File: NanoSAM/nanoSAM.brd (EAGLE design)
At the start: 95.9 x 90.2 mm, 90 parts, among them J1 POWER_JACK, U1 LTC3260EMSEPBF, U2 LMV324

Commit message: added some stuff, fixed some stuff
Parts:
- added C17, C18: 0.1uF, SparkFun-Capacitors:0603
- added C19, C20: .1uF, SparkFun-Capacitors:0603
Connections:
- net +3V3: now also C19.1, C20.2
- net -5V: now also C18.1
- net 5V: now also C17.1
- net AGND: now also C17.2, C18.2
- net DGND: now also C19.2, C20.1
- net SPI_MISO: now also U$16.2, U$17.2; no longer U$16.5, U$17.5
- net SPI_MOSI: now also U$16.5, U$17.5; no longer U$16.6, U$17.6
- net SPI_SCK: now also U$16.6, U$17.6; no longer U$16.2, U$17.2
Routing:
- net SPI_MISO: track 53.8 -> 44.6 mm
- net SPI_SCK: track 88.4 -> 84.6 mm
- net SPI_MOSI: track 26.9 -> 25.4 mm
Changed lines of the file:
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@@
 <attribute name="VALUE" x="72.957" y="65.8" size="0.6096" layer="27" font="vector" ratio="20" rot="R270" align="top-center"/>
+</element>
+<element name="C17" library="SparkFun-Capacitors" library_urn="urn:adsk.eagle:library:510" package="0603" package3d_urn="urn:adsk.eagle:package:37414/1" value="0.1uF" x="-19" y="-2" smashed="yes">
+<attribute name="NAME" x="-19" y="-1.238" size="0.6096" layer="25" font="vector" ratio="20" align="bottom-center"/>
+<attribute name="PROD_ID" value="CAP-08604" x="-19" y="-2" size="1.778" layer="27" display="off"/>
+<attribute name="VALUE" x="-19" y="-2.762" size="0.6096" layer="27" font="vector" ratio="20" align="top-center"/>
+</element>
+<element name="C18" library="SparkFun-Capacitors" library_urn="urn:adsk.eagle:library:510" package="0603" package3d_urn="urn:adsk.eagle:package:37414/1" value="0.1uF" x="-19" y="-6" smashed="yes">
+<attribute name="NAME" x="-19" y="-5.238" size="0.6096" layer="25" font="vector" ratio="20" align="bottom-center"/>
+<attribute name="PROD_ID" value="CAP-08604" x="-19" y="-6" size="1.778" layer="27" display="off"/>
+<attribute name="VALUE" x="-19" y="-6.762" size="0.6096" layer="27" font="vector" ratio="20" align="top-center"/>
+</element>
+<element name="C19" library="SparkFun-Capacitors" library_urn="urn:adsk.eagle:library:510" package="0603" package3d_urn="urn:adsk.eagle:package:37414/1" value=".1uF" x="-19" y="-10" smashed="yes">
+<attribute name="NAME" x="-19" y="-9.238" size="0.6096" layer="25" font="vector" ratio="20" align="bottom-center"/>
+<attribute name="PROD_ID" value="CAP-08604" x="-19" y="-10" size="1.778" layer="27" display="off"/>
+<attribute name="VALUE" x="-19" y="-10.762" size="0.6096" layer="27" font="vector" ratio="20" align="top-center"/>
+</element>
+<element name="C20" library="SparkFun-Capacitors" library_urn="urn:adsk.eagle:library:510" package="0603" package3d_urn="urn:adsk.eagle:package:37414/1" value=".1uF" x="-19" y="-14" smashed="yes">
+<attribute name="NAME" x="-19" y="-13.238" size="0.6096" layer="25" font="vector" ratio="20" align="bottom-center"/>
+<attribute name="PROD_ID" value="CAP-08604" x="-19" y="-14" size="1.778" layer="27" display="off"/>
+<attribute name="VALUE" x="-19" y="-14.762" size="0.6096" layer="27" font="vector" ratio="20" align="top-center"/>
 </element>
 </elements>
@@
 <contactref element="U$5" pad="P6"/>
 <contactref element="U$2" pad="D12"/>
-<contactref element="U$16" pad="5"/>
-<contactref element="U$17" pad="5"/>
-<wire x1="61.07" y1="71.925" x2="52" y2="71.925" width="0.254" layer="1"/>
 <wire x1="52" y1="71.925" x2="39.975" y2="71.925" width="0.254" layer="1"/>
 <wire x1="39.975" y1="71.925" x2="39.5" y2="72.4" width="0.254" layer="1"/>
@@
 <wire x1="54" y1="69.925" x2="54" y2="66" width="0.254" layer="1"/>
 <wire x1="54" y1="66" x2="56" y2="64" width="0.254" layer="1"/>
-<wire x1="61.135" y1="64" x2="61.21" y2="63.925" width="0.254" layer="1"/>
 <wire x1="56" y1="64" x2="61.135" y2="64" width="0.254" layer="1"/>
 <wire x1="51.14" y1="52.43" x2="54" y2="55.29" width="0.254" layer="1"/>
 <wire x1="54" y1="55.29" x2="54" y2="66" width="0.254" layer="1"/>
+<contactref element="U$16" pad="2"/>
+<contactref element="U$17" pad="2"/>
+<wire x1="67.87" y1="61.385" x2="67.73" y2="69.385" width="0" layer="19" extent="1-1"/>
+<wire x1="61.135" y1="64" x2="67.87" y2="61.385" width="0" layer="19" extent="1-1"/>
 </signal>
 <signal name="SPI_SCK">
 <contactref element="U$5" pad="P5"/>
 <contactref element="U$2" pad="D13/LED"/>
-<contactref element="U$16" pad="2"/>
-<contactref element="U$17" pad="2"/>
-<wire x1="67.73" y1="69.385" x2="69.615" y2="69.385" width="0.254" layer="1"/>
 <wire x1="69.615" y1="69.385" x2="70" y2="69" width="0.254" layer="1"/>
 <wire x1="70" y1="69" x2="70" y2="61.6" width="0.254" layer="1"/>
@@
 <wire x1="51.14" y1="38.14" x2="51.14" y2="37.19" width="0.254" layer="1"/>
 <wire x1="70" y1="51" x2="58" y2="39" width="0.254" layer="1"/>
-<wire x1="67.87" y1="61.385" x2="69.785" y2="61.385" width="0.254" layer="1"/>
 <wire x1="69.785" y1="61.385" x2="70" y2="61.6" width="0.254" layer="1"/>
 <wire x1="70" y1="69" x2="70" y2="73" width="0.254" layer="1"/>
@@
 <wire x1="36.1" y1="72.33526875" x2="36.1" y2="73.1" width="0.254" layer="1"/>
 <wire x1="69" y1="74" x2="37" y2="74" width="0.254" layer="1"/>
+<contactref element="U$16" pad="6"/>
+<contactref element="U$17" pad="6"/>
+<wire x1="61.21" y1="62.655" x2="61.07" y2="70.655" width="0" layer="19" extent="1-1"/>
+<wire x1="69" y1="74" x2="61.07" y2="70.655" width="0" layer="19" extent="1-1"/>
 </signal>
 <signal name="SPI_MOSI">
 <contactref element="U$2" pad="D11"/>
-<contactref element="U$16" pad="6"/>
-<contactref element="U$17" pad="6"/>
-<wire x1="61.07" y1="70.655" x2="62.345" y2="70.655" width="0.254" layer="1"/>
 <wire x1="62.345" y1="70.655" x2="63" y2="70" width="0.254" layer="1"/>
 <wire x1="63" y1="70" x2="63" y2="63.5" width="0.254" layer="1"/>
 <wire x1="62" y1="62.5" x2="63" y2="63.5" width="0.254" layer="1"/>
 <wire x1="61.365" y1="62.5" x2="62" y2="62.5" width="0.254" layer="1"/>
-<wire x1="61.365" y1="62.5" x2="61.21" y2="62.655" width="0.254" layer="1"/>
 <wire x1="62.42573125" y1="59.5356" x2="60.7856" y2="59.5356" width="0.254" layer="1"/>
 <wire x1="60.7856" y1="59.5356" x2="53.68" y2="52.43" width="0.254" layer="1"/>
 <wire x1="63" y1="63.5" x2="63" y2="60.10986875" width="0.254" layer="1"/>
 <wire x1="63" y1="60.10986875" x2="62.42573125" y2="59.5356" width="0.254" layer="1"/>
+<contactref element="U$16" pad="5"/>
+<contactref element="U$17" pad="5"/>
+<wire x1="62.345" y1="70.655" x2="61.07" y2="71.925" width="0" layer="19" extent="1-1"/>
+<wire x1="61.21" y1="63.925" x2="61.365" y2="62.5" width="0" layer="19" extent="1-1"/>
 </signal>
 <signal name="N$8">
@@
 <wire x1="11.3" y1="39.6" x2="9.71" y2="38.01" width="0.508" layer="16"/>
 <wire x1="6.16" y1="38.01" x2="9.71" y2="38.01" width="0.508" layer="16"/>
+<contactref element="C17" pad="1"/>
+<wire x1="-19.85" y1="-2" x2="6.16" y2="22.24" width="0" layer="19" extent="1-1"/>
 </signal>
 <signal name="AGND">
@@
 <wire x1="14.9" y1="63.1" x2="14.8" y2="63" width="0.508" layer="16"/>
 <wire x1="14.8" y1="63" x2="11.3" y2="63" width="0.508" layer="16"/>
+<contactref element="C17" pad="2"/>
+<contactref element="C18" pad="2"/>
+<wire x1="-18.15" y1="-2" x2="-18.15" y2="-6" width="0" layer="19" extent="1-1"/>
+<wire x1="9.4" y1="11.5" x2="-18.15" y2="-2" width="0" layer="19" extent="1-1"/>
 </signal>
 <signal name="DGND">
@@
 <wire x1="83.265" y1="67.265" x2="83.3" y2="67.3" width="0.254" layer="1"/>
 <via x="83.3" y="67.3" extent="1-16" drill="0.35"/>
+<contactref element="C19" pad="2"/>
+<contactref element="C20" pad="1"/>
 <wire x1="72.6" y1="17.2" x2="71.098" y2="17.768" width="0" layer="19" extent="1-1"/>
+<wire x1="-18.15" y1="-10" x2="32.845" y2="3.68" width="0" layer="19" extent="1-1"/>
+<wire x1="-19.85" y1="-14" x2="-18.15" y2="-10" width="0" layer="19" extent="1-1"/>
 </signal>
 <signal name="+3V3" class="2">
@@
 <wire x1="73.9" y1="67" x2="72" y2="67" width="0.254" layer="1"/>
 <via x="72" y="67" extent="1-16" drill="0.35"/>
+<contactref element="C19" pad="1"/>
+<contactref element="C20" pad="2"/>
+<wire x1="-19.85" y1="-10" x2="-18.15" y2="-14" width="0" layer="19" extent="1-1"/>
+<wire x1="32.3406" y1="3.06426875" x2="-18.15" y2="-14" width="0" layer="19" extent="1-1"/>
 </signal>
 <signal name="VBUS">
@@
 <wire x1="19.9" y1="51.9" x2="20.3" y2="52.3" width="0.508" layer="16"/>
 <wire x1="20.3" y1="52.3" x2="20.3" y2="53" width="0.508" layer="16"/>
+<contactref element="C18" pad="1"/>
+<wire x1="-19.85" y1="-6" x2="19.55" y2="27.61" width="0" layer="19" extent="1-1"/>
 </signal>
 <signal name="N$22">

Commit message: updated some stuff
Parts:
- C1: value 0.1uF -> 100pF
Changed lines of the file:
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@@
 </autorouter>
 <elements>
-<element name="C1" library="SparkFun-Capacitors" library_urn="urn:adsk.eagle:library:510" package="0603" package3d_urn="urn:adsk.eagle:package:37414/1" value="0.1uF" x="21.79" y="72.05" smashed="yes" rot="R270">
+<element name="C1" library="SparkFun-Capacitors" library_urn="urn:adsk.eagle:library:510" package="0603" package3d_urn="urn:adsk.eagle:package:37414/1" value="100pF" x="21.79" y="72.05" smashed="yes" rot="R270">
 <attribute name="NAME" x="20.852" y="75.05" size="1.778" layer="25" font="vector" ratio="20" rot="R270" align="bottom-center"/>
 <attribute name="PROD_ID" value="CAP-08604" x="-37.9" y="53" size="1.778" layer="27" rot="R270" display="off"/>

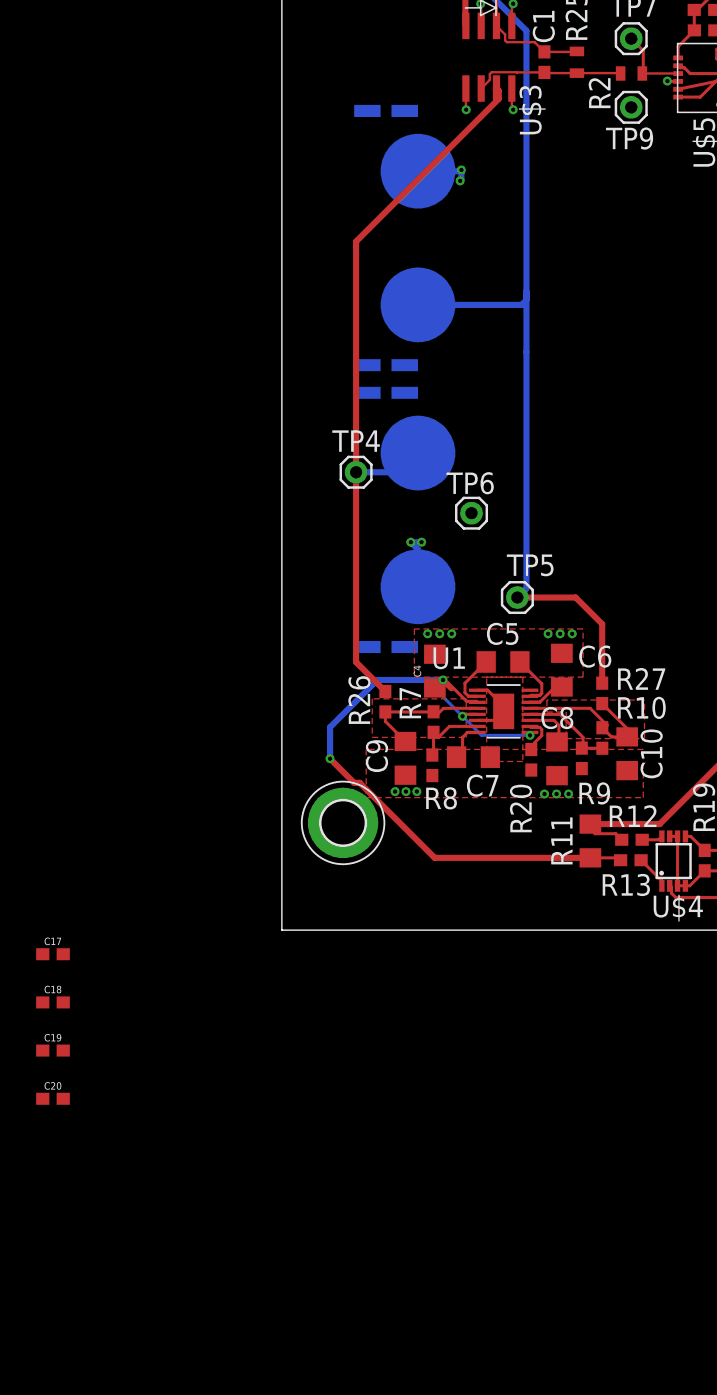
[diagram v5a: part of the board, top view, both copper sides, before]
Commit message: added options for grounding ADCs
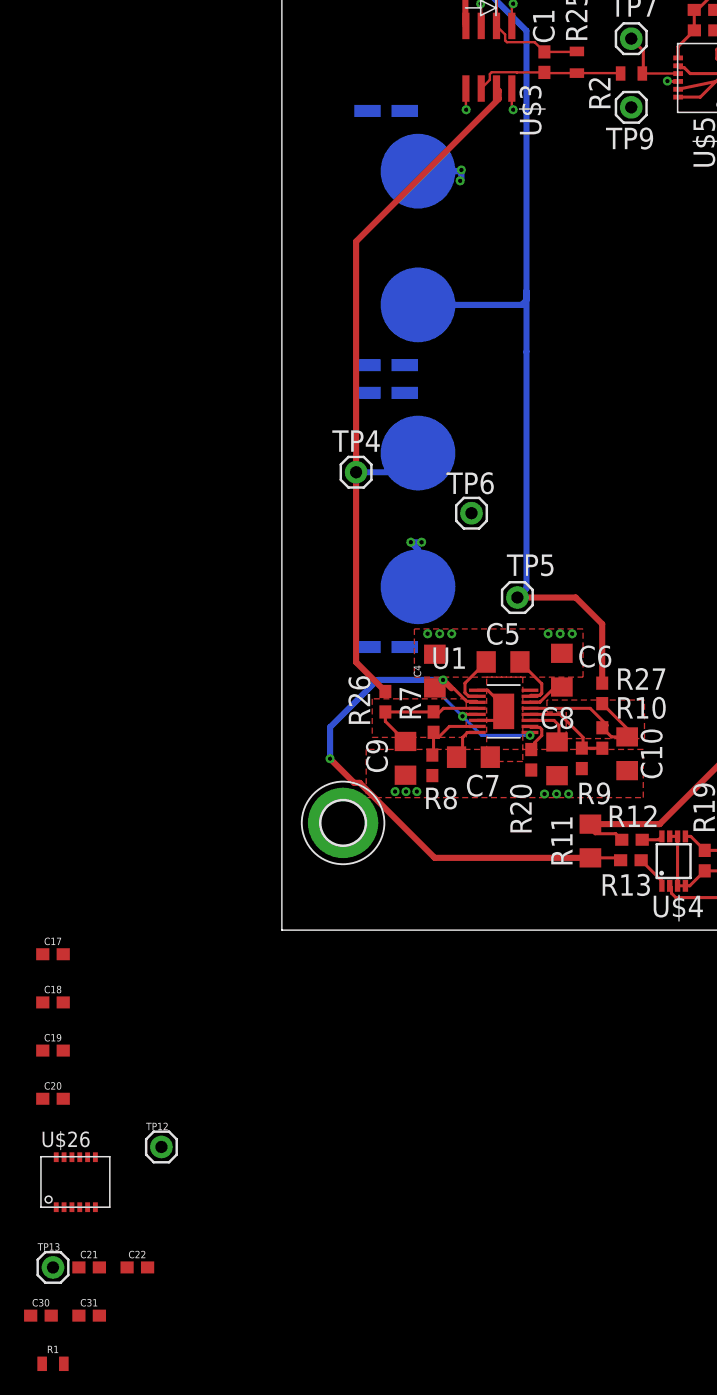
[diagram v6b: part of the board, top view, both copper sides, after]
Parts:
- added C21, C22, C30, C31: 0.1uF, SparkFun-Capacitors:0603
- added R1: 0, SparkFun-Resistors:0805
- added TP12, TP13: (no value), testpoint:1X01
- added U$26: LTC2470, LTC2470:MSOP12
- R2: value (none) -> 0
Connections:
- new net N$25: C21.2, U$26.P1
- new net N$26: C30.1, C31.1, U$26.P7
- new net N$5: R2.2, TP12.1, U$26.P9
- new net N$9: C22.2, U$26.P2
- net ADC_CS: now also U$26.P3
- net AGND: now also C21.1, C22.1, C30.2, C31.2, TP13.1, U$26.P10, U$26.P11, U$26.P12, U$26.P4, U$26.P8
- net N$2: now also R1.1
- net N$3: now also R1.2; no longer R2.2
- net SPI_MISO: now also U$26.P6
- net SPI_SCK: now also U$26.P5

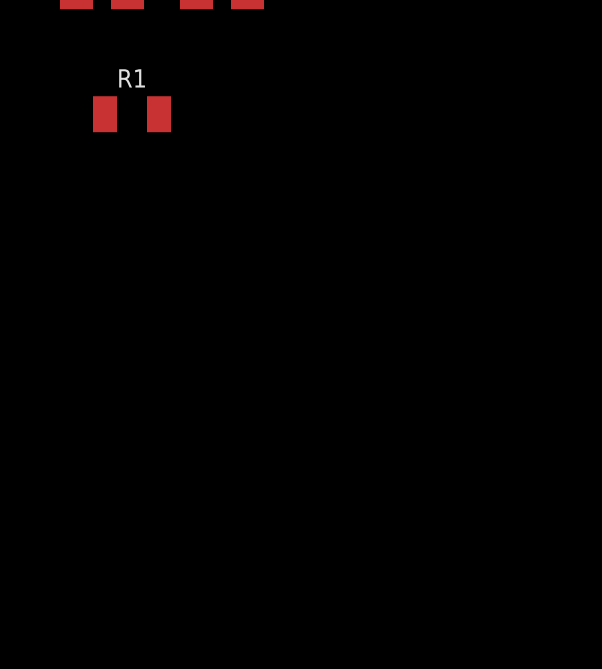
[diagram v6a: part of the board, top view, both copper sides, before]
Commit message: Added analog grounded ADC power regulator
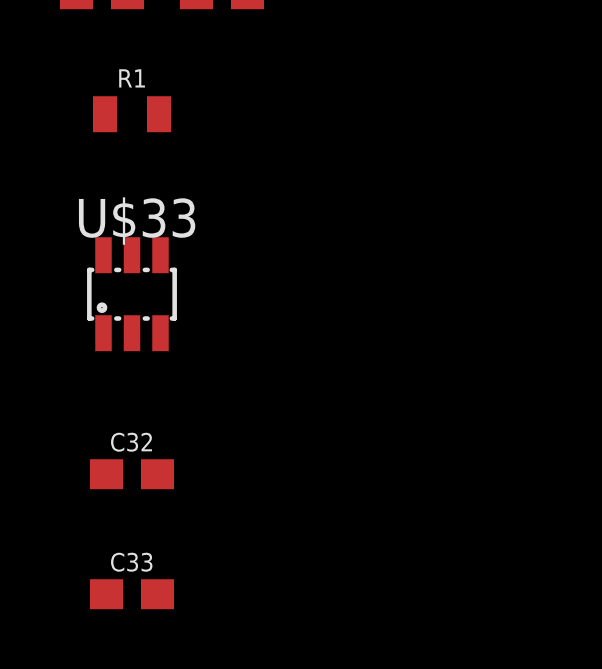
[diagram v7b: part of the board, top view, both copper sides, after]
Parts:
- added C32: 0.1uF, SparkFun-Capacitors:0603
- added C33: 1uF, SparkFun-Capacitors:0603
- added U$33: LT6654-3.3, LT6654:SOT23-6L
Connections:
- net 5V: now also C32.1, U$33.4
- net AGND: now also C32.2, C33.2, U$33.1, U$33.2
- net N$26: now also C33.1, U$33.6
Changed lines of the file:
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@@
 <attribute name="VALUE" x="-19" y="-36.889" size="0.6096" layer="27" font="vector" ratio="20" align="top-center"/>
+</element>
+<element name="U$33" library="LT6654" package="SOT23-6L" value="LT6654-3.3" x="-19" y="-42" smashed="yes">
+<attribute name="NAME" x="-20.905" y="-40.095" size="1.27" layer="25"/>
+<attribute name="VALUE" x="-20.905" y="-45.175" size="1.27" layer="27"/>
+</element>
+<element name="C32" library="SparkFun-Capacitors" library_urn="urn:adsk.eagle:library:510" package="0603" package3d_urn="urn:adsk.eagle:package:37414/1" value="0.1uF" x="-19" y="-48" smashed="yes">
+<attribute name="NAME" x="-19" y="-47.238" size="0.6096" layer="25" font="vector" ratio="20" align="bottom-center"/>
+<attribute name="PROD_ID" value="CAP-08604" x="-19" y="-48" size="1.778" layer="27" display="off"/>
+<attribute name="VALUE" x="-19" y="-48.762" size="0.6096" layer="27" font="vector" ratio="20" align="top-center"/>
+</element>
+<element name="C33" library="SparkFun-Capacitors" library_urn="urn:adsk.eagle:library:510" package="0603" package3d_urn="urn:adsk.eagle:package:37414/1" value="1uF" x="-19" y="-52" smashed="yes">
+<attribute name="NAME" x="-19" y="-51.238" size="0.6096" layer="25" font="vector" ratio="20" align="bottom-center"/>
+<attribute name="PROD_ID" value="CAP-08604" x="-19" y="-52" size="1.778" layer="27" display="off"/>
+<attribute name="VALUE" x="-19" y="-52.762" size="0.6096" layer="27" font="vector" ratio="20" align="top-center"/>
 </element>
 </elements>
@@
 <wire x1="6.16" y1="38.01" x2="9.71" y2="38.01" width="0.508" layer="16"/>
 <contactref element="C17" pad="1"/>
-<wire x1="-19.85" y1="-2" x2="6.16" y2="22.24" width="0" layer="19" extent="1-1"/>
+<contactref element="U$33" pad="4"/>
+<contactref element="C32" pad="1"/>
+<wire x1="-18.05" y1="-40.7" x2="-19.85" y2="-48" width="0" layer="19" extent="1-1"/>
+<wire x1="-19.85" y1="-2" x2="-18.05" y2="-40.7" width="0" layer="19" extent="1-1"/>
+<wire x1="6.16" y1="22.24" x2="-19.85" y2="-2" width="0" layer="19" extent="1-1"/>
 </signal>
 <signal name="AGND">
@@
 <contactref element="C22" pad="1"/>
 <contactref element="C21" pad="1"/>
+<contactref element="C33" pad="2"/>
+<contactref element="C32" pad="2"/>
+<contactref element="U$33" pad="1"/>
+<contactref element="U$33" pad="2"/>
 <wire x1="29" y1="68.3" x2="32" y2="70.4794" width="0" layer="19" extent="1-1"/>
 <wire x1="19.2" y1="68.1" x2="29" y2="68.3" width="0" layer="19" extent="1-1"/>
@@
 <wire x1="-15.15" y1="-32" x2="-19.15" y2="-32" width="0" layer="19" extent="1-1"/>
 <wire x1="-12.85" y1="-28" x2="-16.85" y2="-28" width="0" layer="19" extent="1-1"/>
+<wire x1="-19" y1="-43.3" x2="-19.15" y2="-32" width="0" layer="19" extent="1-1"/>
+<wire x1="-19.95" y1="-43.3" x2="-19" y2="-43.3" width="0" layer="19" extent="1-1"/>
+<wire x1="-18.15" y1="-48" x2="-19" y2="-43.3" width="0" layer="19" extent="1-1"/>
+<wire x1="-18.15" y1="-52" x2="-18.15" y2="-48" width="0" layer="19" extent="1-1"/>
 </signal>
 <signal name="DGND">
@@
 <contactref element="C30" pad="1"/>
 <contactref element="C31" pad="1"/>
+<contactref element="U$33" pad="6"/>
+<contactref element="C33" pad="1"/>
+<wire x1="-19.95" y1="-40.7" x2="-19.85" y2="-52" width="0" layer="19" extent="1-1"/>
+<wire x1="-20.85" y1="-32" x2="-19.95" y2="-40.7" width="0" layer="19" extent="1-1"/>
 <wire x1="-16.85" y1="-32" x2="-20.85" y2="-32" width="0" layer="19" extent="1-1"/>
 <wire x1="-15.48" y1="-18.85" x2="-16.85" y2="-32" width="0" layer="19" extent="1-1"/>

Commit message: Finished fixing stuff
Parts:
- added R28, R31, R37, R38, R39, R5: 49.99, SparkFun-Resistors:0805
- C25, C26: value 47uF -> 47uF - 10V
- R22: value 230k -> 240k
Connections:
- removed net 6V_PWR_ENA: U$12.P4
- removed net N$43: U$12.P7
- removed net PWR_6V_PG: U$12.P15
- new net HK_3V3_PG: U$12.P15, U$2.D0
- new net N$30: R5.1, U$5.P6
- new net N$33: R28.1, U$26.P6
- new net N$38: R31.2, U$2.D11
- new net N$39: R37.1, U$2.D13/LED
- new net N$40: R38.2, U$16.2
- new net N$41: R39.2, U$17.2
- net DGND: now also U$12.P7, U$2.AGND
- net N$84: now also U$12.P4
- net SPI_MISO: now also R28.2, R38.1, R39.1, R5.2; no longer U$16.2, U$17.2, U$26.P6, U$5.P6
- net SPI_MOSI: now also R31.1; no longer U$2.D11
- net SPI_SCK: now also R37.2; no longer U$2.D13/LED
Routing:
- net SPI_MOSI: track 25.4 -> 0.00 mm
- net N$38: track 0.00 -> 25.4 mm
- net SPI_MISO: track 44.6 -> 42.2 mm
- net SPI_SCK: track 84.6 -> 83.7 mm
